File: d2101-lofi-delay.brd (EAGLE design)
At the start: 100 x 50 mm, 84 parts, among them U1 FX2-20P-1.27DS, U2 FX2-20S-1.27DS

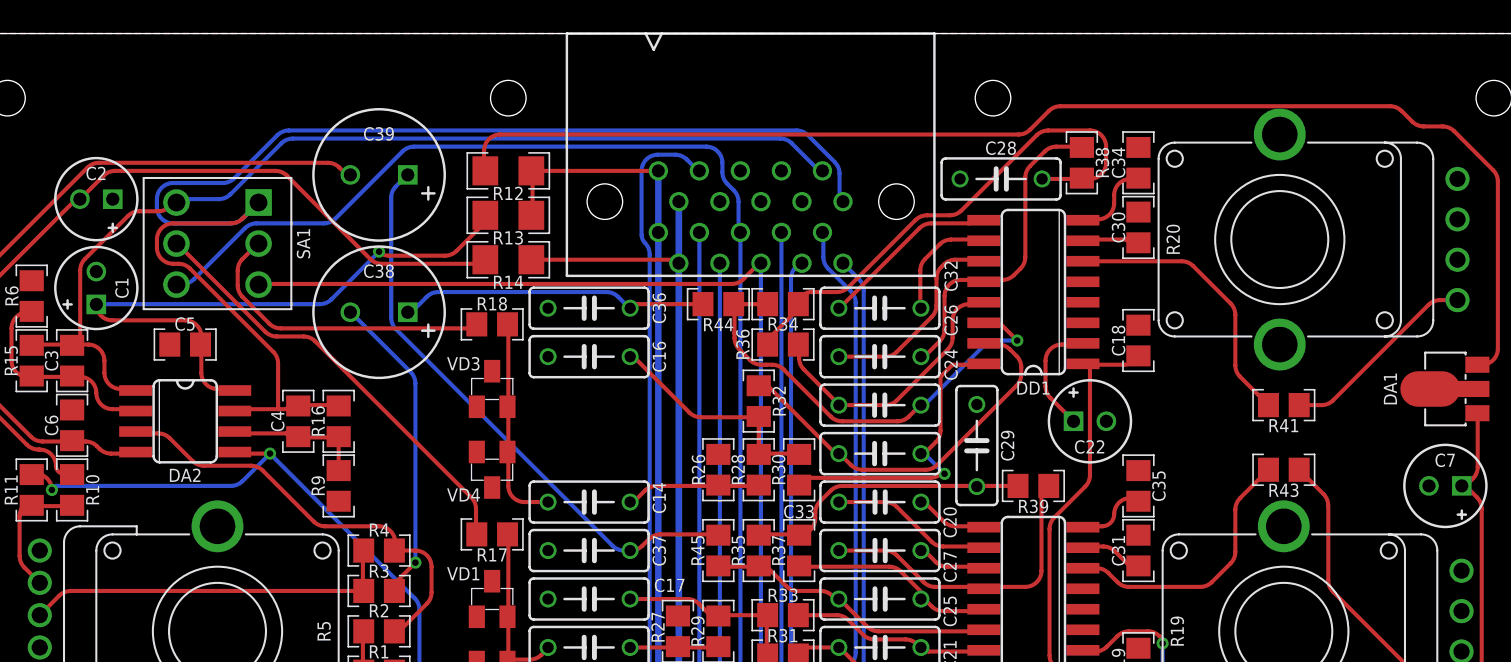
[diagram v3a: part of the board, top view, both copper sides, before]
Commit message: Replace 10R with ferrite bead Replace 47u/35V with 33u/25V
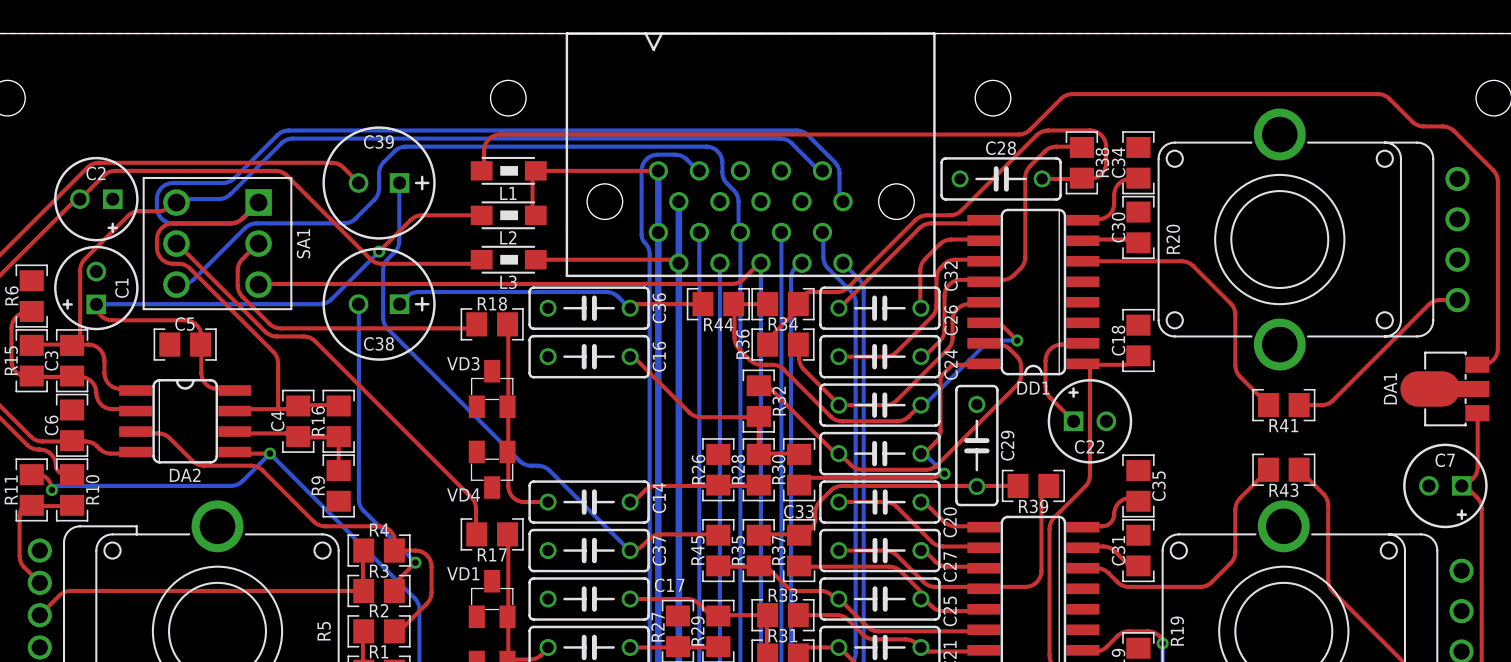
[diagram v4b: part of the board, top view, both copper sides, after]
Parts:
- removed R12, R13, R14: 10R(1206), resistors:R-1206
- added L1, L2, L3: BLM31AJ601SN1L, inductors:1206
- C38, C39: value 47U/35V -> 33U/25V; device capacitors-electrolytic:E3,5-8 -> capacitors-electrolytic:E2,5-7
- DA1: value NJM78L05UA -> L78L05ACU
- moved C38 0.50 mm to (27.0, 33.2)
- moved C39 0.50 mm to (27.0, 40.8)
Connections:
- net +15V: now also L2.2; no longer R13.2
- net -15V: now also L3.2; no longer R14.2
- net N$36: now also L3.1; no longer R14.1
- net N$44: now also L1.2; no longer R12.2
- net P+15V: now also L1.1, L2.1; no longer R12.1, R13.1
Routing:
- net FBK_LEFT: track 72.5 -> 73.4 mm
- net OUT_LEFT: track 41.4 -> 42.2 mm
- net N$44: track 79.0 -> 79.7 mm
- net +15V: track 38.8 -> 38.3 mm

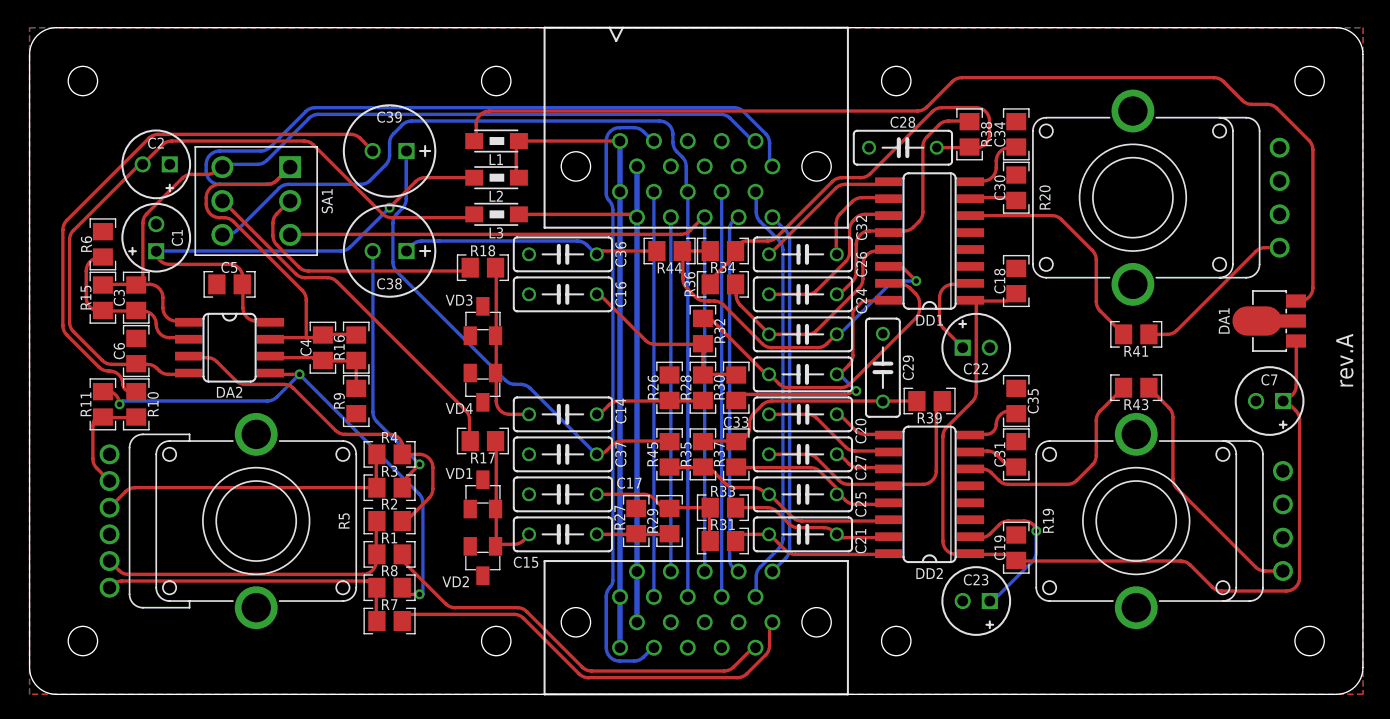
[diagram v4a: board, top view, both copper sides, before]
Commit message: Replace feedback switch with MJS22R
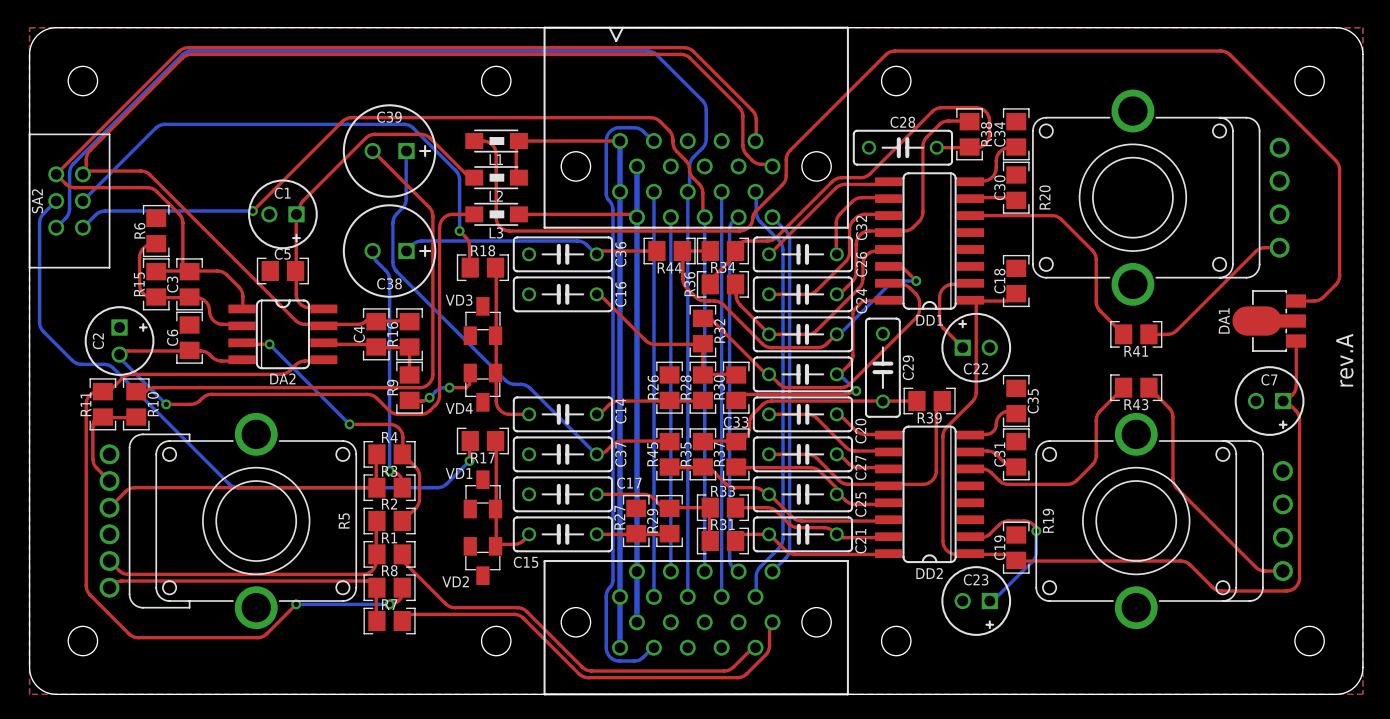
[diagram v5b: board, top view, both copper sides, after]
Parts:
- removed SA1: 108-0052-EVX, switches:108-0052-EVX
- added SA2: MJS22R, switches:APEM-MJS22R
- moved C2 13.5 mm to (6.75, 26.5), turned to 270 degrees
- moved C1 9.66 mm to (19.0, 36.0), turned to 180 degrees
- moved C3 4.12 mm to (12.0, 30.8)
- moved C4 4.12 mm to (26.0, 27.0)
- moved C5 4.12 mm to (19.0, 31.8)
- moved C6 4.12 mm to (12.0, 26.8)
- moved DA2 4.12 mm to (19.0, 27.0)
- moved R15 4.12 mm to (9.50, 30.8)
- moved R16 4.12 mm to (28.5, 27.0)
- moved R6 4.12 mm to (9.50, 34.8)
- moved R9 4.12 mm to (28.5, 23.0)
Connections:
- net FBK_INT_LEFT: now also SA2.NC1; no longer SA1.4
- net FBK_INT_RIGHT: now also SA2.NC2; no longer SA1.1
- net FBK_LEFT: now also SA2.NO1; no longer SA1.6
- net FBK_RIGHT: now also SA2.NO2; no longer SA1.3
- net N$13: now also SA2.C2; no longer SA1.2
- net N$6: now also SA2.C1; no longer SA1.5
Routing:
- net FBK_RIGHT: track 58.1 -> 81.4 mm, vias 0 -> 1
- net N$6: track 27.0 -> 49.2 mm, vias 0 -> 1
- net FBK_LEFT: track 73.4 -> 95.0 mm
- net FBK_INT_LEFT: track 63.3 -> 84.0 mm
- net N$13: track 19.6 -> 39.3 mm, vias 0 -> 1
- net N$39: track 40.7 -> 59.8 mm, vias 3 -> 2
- net N$44: track 79.7 -> 93.1 mm
- net +15V: track 38.3 -> 26.1 mm, vias 1 -> 0
- net FBK_INT_RIGHT: track 82.4 -> 90.2 mm
- net GND: track 0.00 -> 5.81 mm, vias 0 -> 2
- net N$61: track 27.6 -> 22.3 mm, vias 0 -> 2
- net -15V: track 53.5 -> 52.2 mm, vias 0 -> 1
- net OUT_RIGHT: track 19.7 -> 18.6 mm
- net OUT_LEFT: track 42.2 -> 41.3 mm

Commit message: d2101 controls placement fix
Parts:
- moved C2 33.3 mm to (40.0, 25.5)
- moved C39 32.8 mm to (28.0, 8.00)
- moved R2 27.6 mm to (7.00, 32.0), turned to 180 degrees
- moved R8 27.5 mm to (25.5, 35.5), turned to 90 degrees
- moved C38 26.1 mm to (20.5, 8.00)
- moved R11 22.3 mm to (23.0, 35.5)
- moved R4 21.7 mm to (8.00, 28.5), turned to 90 degrees
- moved R10 20.5 mm to (27.0, 14.0), turned to 90 degrees
- moved C4 13.3 mm to (23.0, 40.0)
- moved R16 13.3 mm to (25.5, 40.0)
- moved R9 12.5 mm to (28.0, 35.5)
- moved C5 12.5 mm to (16.5, 44.0)
- moved DA2 12.5 mm to (16.5, 39.2)
- moved R5 12.0 mm to (17.0, 25.0), turned to 90 degrees
- moved SA2 12.0 mm to (0.00, 25.0)
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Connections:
- net FBK_INT_LEFT: now also SA2.NO1; no longer SA2.NC1
- net FBK_INT_RIGHT: now also SA2.NO2; no longer SA2.NC2
- net FBK_LEFT: now also SA2.NC1; no longer SA2.NO1
- net FBK_RIGHT: now also SA2.NC2; no longer SA2.NO2
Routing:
- net N$39: track 59.8 -> 6.24 mm, vias 2 -> 0
- net OUT_LEFT: track 41.3 -> 5.12 mm, vias 0 -> 1
- net N$57: track 19.5 -> 47.9 mm
- net FBK_INT_RIGHT: track 90.2 -> 71.2 mm, vias 0 -> 3
- net N$65: track 23.2 -> 41.9 mm, vias 0 -> 1
- net N$40: track 8.35 -> 23.0 mm, vias 0 -> 1
- net N$30: track 23.9 -> 37.1 mm, vias 0 -> 1
- net OUT_RIGHT: track 18.6 -> 5.94 mm, vias 1 -> 0
- net N$28: track 33.0 -> 45.5 mm, vias 0 -> 1
- net N$24: track 35.8 -> 26.3 mm
- net FBK_RIGHT: track 81.4 -> 89.9 mm
- net FBK_LEFT: track 95.0 -> 103.1 mm
- net N$13: track 39.3 -> 32.2 mm, vias 1 -> 0
- net N$61: track 22.3 -> 15.7 mm, vias 2 -> 0
- net +15V: track 26.1 -> 20.0 mm
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
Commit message: Changed 47u/16V -> 10u/35V
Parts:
- C22, C23, C7: value 47U/16V -> 10U/35V
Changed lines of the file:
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@@
 <attribute name="NAME" x="11.27" y="35.5" size="0.8128" layer="25" ratio="15" rot="R270" align="center"/>
 </element>
-<element name="C7" library="capacitors-electrolytic" package="E2-5" value="47U/16V" x="93" y="22" smashed="yes" rot="R180">
-<attribute name="MOUSER" value="647-USW1C470MDD" x="186" y="53" size="1.778" layer="27" rot="R180" display="off"/>
+<element name="C7" library="capacitors-electrolytic" package="E2-5" value="10U/35V" x="93" y="22" smashed="yes" rot="R180">
+<attribute name="MOUSER" value="647-USW1V100MDD" x="186" y="53" size="1.778" layer="27" rot="R180" display="off"/>
 <attribute name="NAME" x="93" y="23.5875" size="0.8128" layer="25" ratio="15" rot="R180" align="center"/>
 </element>
@@
 <attribute name="NAME" x="72.77" y="11" size="0.8128" layer="25" ratio="15" rot="R270" align="center"/>
 </element>
-<element name="C23" library="capacitors-electrolytic" package="E2-5" value="47U/16V" x="71" y="7" smashed="yes" rot="R180">
-<attribute name="MOUSER" value="647-USW1C470MDD" x="183" y="90" size="1.778" layer="27" rot="R180" display="off"/>
+<element name="C23" library="capacitors-electrolytic" package="E2-5" value="10U/35V" x="71" y="7" smashed="yes" rot="R180">
+<attribute name="MOUSER" value="647-USW1V100MDD" x="183" y="90" size="1.778" layer="27" rot="R180" display="off"/>
 <attribute name="NAME" x="71" y="8.5875" size="0.8128" layer="25" ratio="15" rot="R180" align="center"/>
 </element>
@@
 <attribute name="NAME" x="72.77" y="31" size="0.8128" layer="25" ratio="15" rot="R270" align="center"/>
 </element>
-<element name="C22" library="capacitors-electrolytic" package="E2-5" value="47U/16V" x="71" y="26" smashed="yes">
-<attribute name="MOUSER" value="647-USW1C470MDD" x="-133" y="-197" size="1.778" layer="27" display="off"/>
+<element name="C22" library="capacitors-electrolytic" package="E2-5" value="10U/35V" x="71" y="26" smashed="yes">
+<attribute name="MOUSER" value="647-USW1V100MDD" x="-133" y="-197" size="1.778" layer="27" display="off"/>
 <attribute name="NAME" x="71" y="24.4125" size="0.8128" layer="25" ratio="15" align="center"/>
 </element>
